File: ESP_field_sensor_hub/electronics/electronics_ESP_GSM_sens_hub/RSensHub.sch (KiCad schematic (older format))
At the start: 39 parts, among them J1 RJ45_Shielded, J2 RJ45_Shielded, J3 Conn_01x02_Female, J4 Conn_01x04_Female, Q1 IRF3205, Q2 IRF3205, Q3 IRF3205, Q4 IRF3205, Q5 IRF3205, Q6 IRF3205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

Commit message: Previous
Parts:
- added D? (x2): LED, symbol Device:LED
- added R? (x2): R, myComponents:resistor0.25,9mm, symbol Device:R
- added SW?: SW_DIP_x03, symbol Switch:SW_DIP_x03
- U4: footprint (none) -> myComponents:sim7000G_dev_board
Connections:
- net labels added: COM_IN_LED, COM_OUT_LED, SIM_IN_LED, SIM_OUT_LED
- wire segments 149 -> 182
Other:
- moved on the sheet: C1, D1, D2, D3, D4, D5, R1, R13, R14, R2, R4, R8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

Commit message: worked on sens hub PCB
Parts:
- removed D? (x2): LED, symbol Device:LED
- removed R?: R, myComponents:resistor0.25,9mm, symbol Device:R
- removed SW1, SW?: SW_DIP_x03, symbol Switch:SW_DIP_x03
- added AE1: Antenna, myComponents:GNSSantennaVertical, symbol Device:Antenna
- added C2: 1000u16V, myComponents:CAP_Radial_D10.0mm_P5.00mm, symbol Device:CP1
- added D6, D7: LED, myComponents:LED_small_D3.0mm, symbol Device:LED
- added J5: Barrel_Jack_MountingPin, symbol Connector:Barrel_Jack_MountingPin
- added J6: Conn_01x04_Female, myComponents:TerminalBlockRemovablex4, symbol Connector:Conn_01x04_Female
- added JP3, JP4, JP5, JP6: Jumper_2_Bridged, myComponents:jumperx2_P2.54mm_widePads, symbol Jumper:Jumper_2_Bridged
- added R17: R, myComponents:resistor0.25,9mm, symbol Device:R
- D1, D2, D4, D5: footprint (none) -> myComponents:LED_small_D3.0mm
- JP2: footprint (none) -> Jumper:SolderJumper-2_P1.3mm_Open_RoundedPad1.0x1.5mm
- gave numbers to parts that had none: 1
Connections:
- wire segments 182 -> 178
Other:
- moved on the sheet: D1, J4, JP1, R1, R18, R2, U1

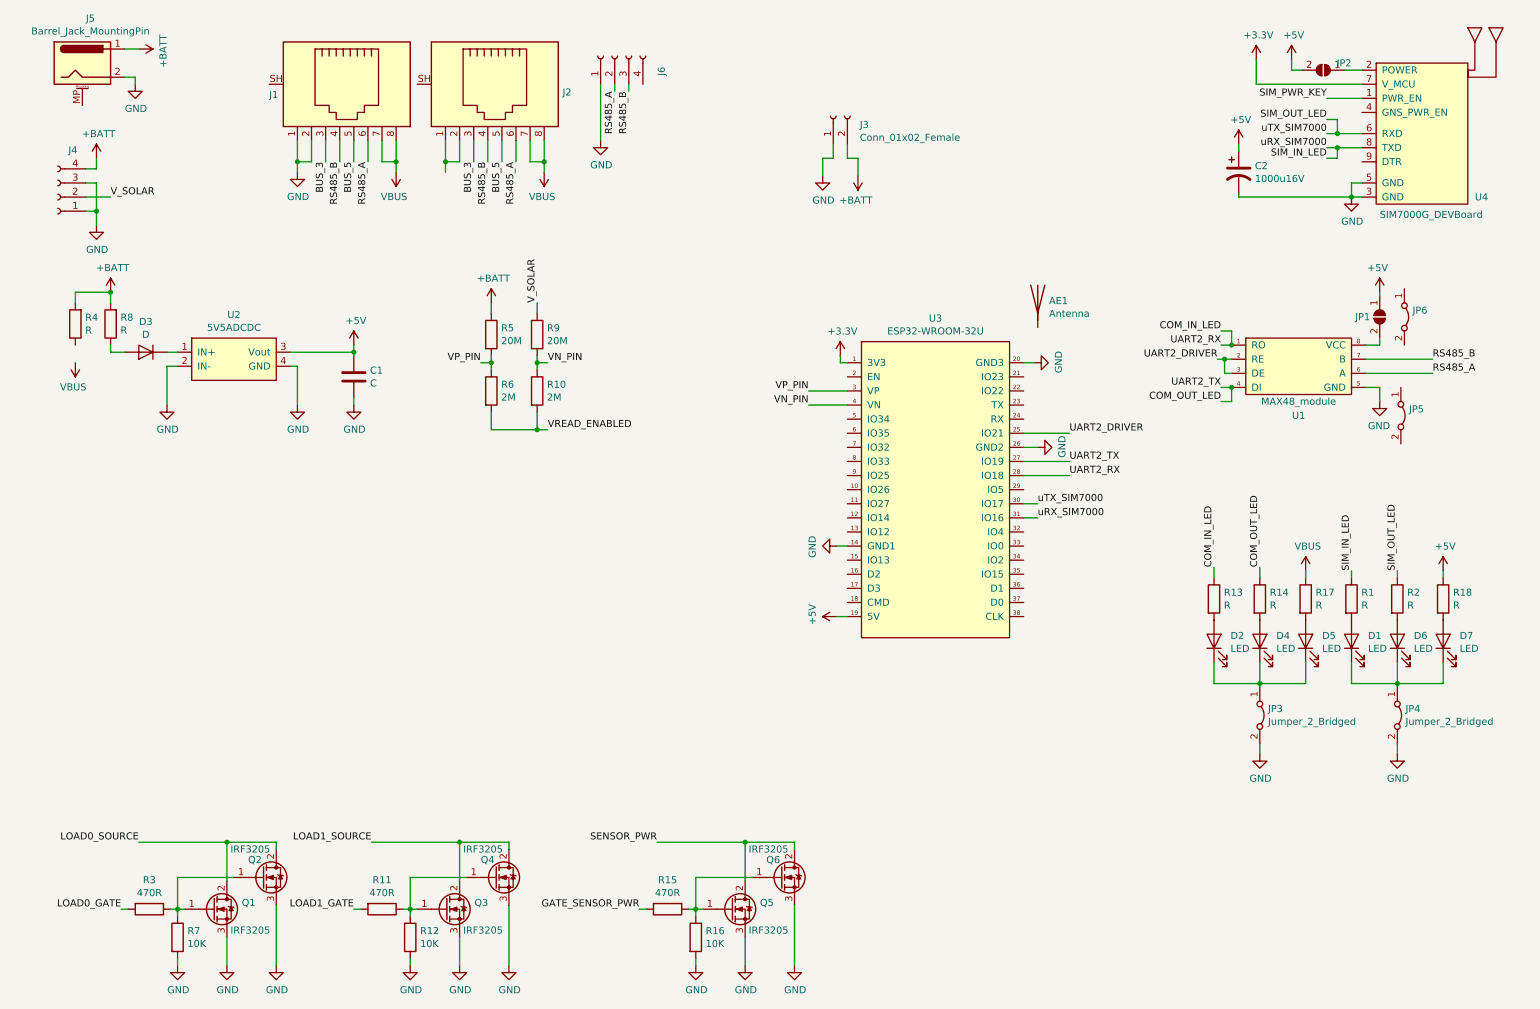
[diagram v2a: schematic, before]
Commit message: short circuit protection - tested on dot board, ESP control pins not connected
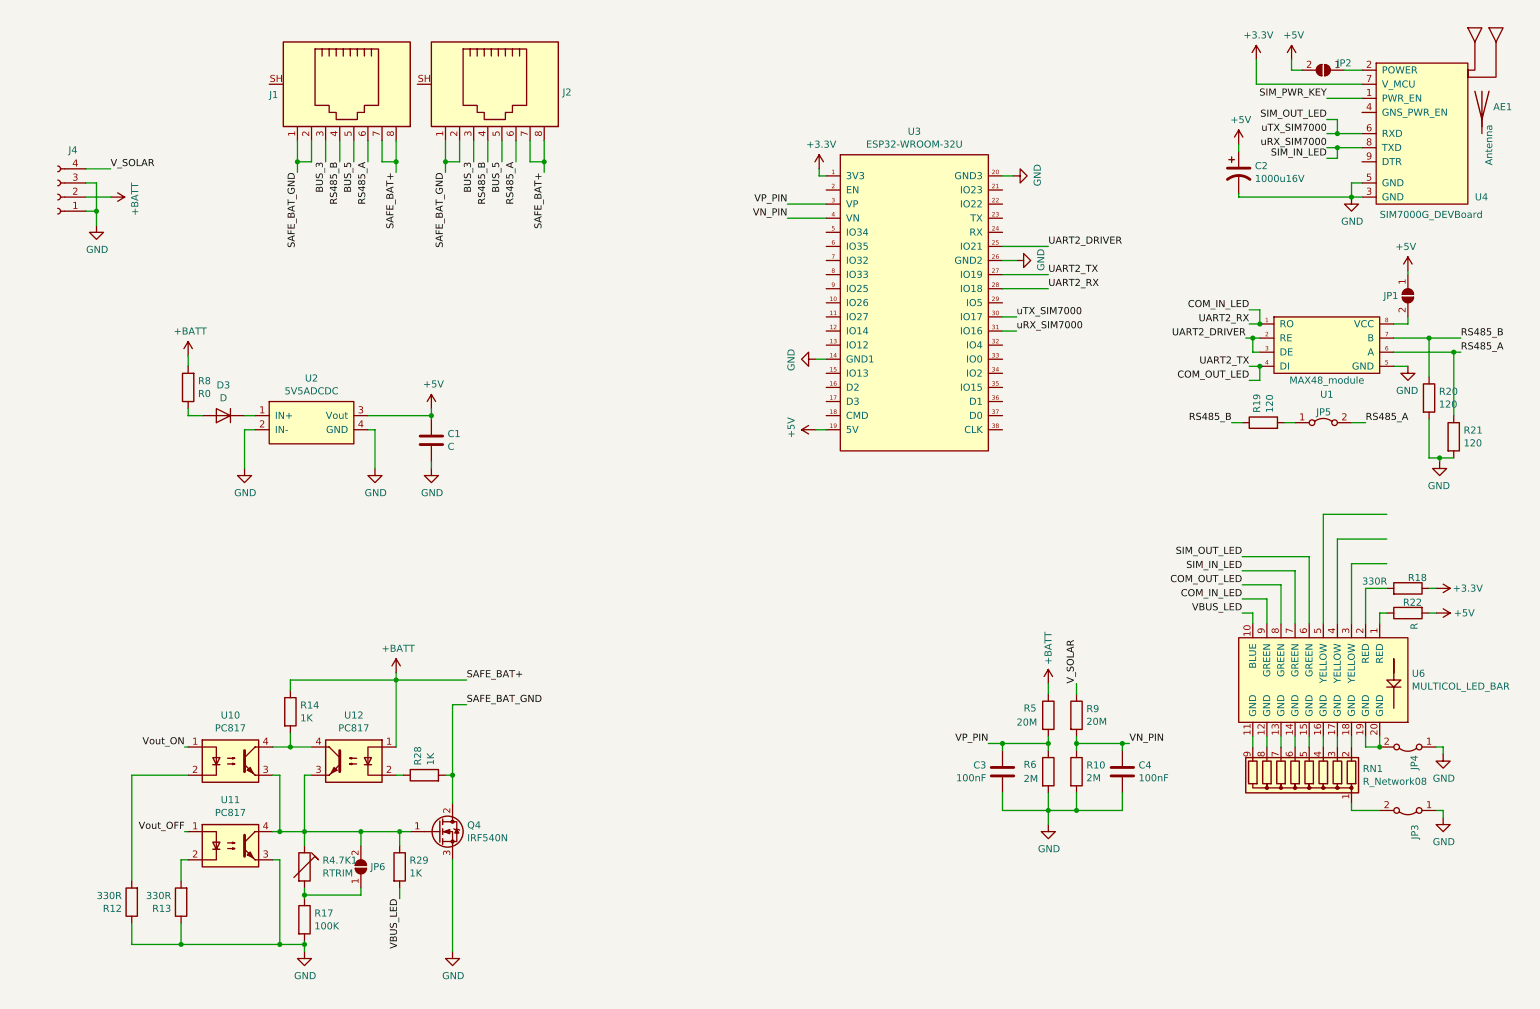
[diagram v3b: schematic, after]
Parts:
- removed D1, D2, D4, D5, D6, D7: LED, myComponents:LED_small_D3.0mm, symbol Device:LED
- removed J3: Conn_01x02_Female, symbol Connector:Conn_01x02_Female
- removed J5: Barrel_Jack_MountingPin, symbol Connector:Barrel_Jack_MountingPin
- removed J6: Conn_01x04_Female, myComponents:TerminalBlockRemovablex4, symbol Connector:Conn_01x04_Female
- removed JP6: Jumper_2_Bridged, myComponents:jumperx2_P2.54mm_widePads, symbol Jumper:Jumper_2_Bridged
- removed Q1, Q2, Q3, Q4, Q5, Q6: IRF3205, Package_TO_SOT_THT:TO-220-3_Vertical, symbol Transistor_FET:IRF3205
- removed R1, R2: R, myComponents:resistor0.25,9mm, symbol Device:R
- removed R11, R15, R3: 470R, myComponents:resistor0.25,9mm, symbol Device:R
- removed R16, R7: 10K, myComponents:resistor0.25,9mm, symbol Device:R
- removed R4: R, symbol Device:R
- added C3, C4: 100nF, myComponents:Capker_L4.6mm_W2.0mm_P2.50mm, symbol Device:C
- added JP6: SolderJumper_2_Open, Jumper:SolderJumper-2_P1.3mm_Open_RoundedPad1.0x1.5mm, symbol Jumper:SolderJumper_2_Open
- added Q4: IRF540N, myComponents:TO-220-3_Horizontal_TabDown_bothSides, symbol Transistor_FET:IRF540N
- added R19, R20, R21: 120, myComponents:resistor0.25,9mm, symbol Device:R
- added R22: R, myComponents:resistor0.25,9mm, symbol Device:R
- added R28, R29: 1K, myComponents:resistor0.25,9mm, symbol Device:R
- added R4.7K1: RTRIM, symbol Device:RTRIM
- added RN1: R_Network08, myComponents:PinHeader_1x9_P2.54mm_widePads, symbol Device:R_Network08
- added U10, U11, U12: PC817, myComponents:optoCouplerDIP4, symbol Isolator:PC817
- added U6: MULTICOL_LED_BAR, myComponents:DIP-20_LED_BAR_DISP, symbol myComponents:MULTICOL_LED_BAR
- JP1: footprint (none) -> Jumper:SolderJumper-2_P1.3mm_Open_RoundedPad1.0x1.5mm
- JP5: value Jumper_2_Bridged -> RS485 terminator
- R12: value 10K -> 330R
- R13, R18: value R -> 330R
- R14: value R -> 1K
- R17: value R -> 100K
- R8: value R -> R0; footprint (none) -> myComponents:resistor0.25,9mm
- U2: footprint (none) -> myComponents:DCDC_HCW_P715
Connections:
- net VREAD_ENABLED is gone; now on net GND: R10.2, R6.2
- net +3V3: now also R18.1
- net +5V: now also R22.2; no longer R18.1
- net +BATT: now also J1.7, J1.8, J2.7, J2.8, J4.2 (Pin_2), R14.1, U12.1; no longer J4.4 (Pin_4)
- net COM_IN_LED: now also U6.9 (GREEN); no longer R13.1
- net COM_OUT_LED: now also U6.8 (GREEN); no longer R14.1
- net GND: now also JP3.1 (A), JP4.1 (A), R12.1, R13.1, R17.2, C3.2, C4.2, Q4.3 (S), R20.2, R21.2, U11.3; no longer J1.1, J1.2, JP3.2 (B), JP4.2 (B), R12.2
- net RS485_A: now also JP5.2 (B), R21.1
- net RS485_B: now also R19.1, R20.1
- net SIM_IN_LED: now also U6.7 (GREEN)
- net SIM_OUT_LED: now also U6.6 (GREEN)
- net VN_PIN: now also C4.1
- net VP_PIN: now also C3.1
- net V_SOLAR: now also J4.4 (Pin_4); no longer J4.2 (Pin_2)
- net SAFE_BAT_GND: now reaches J2.1, J2.2
- net SAFE_BAT_GND: now also J1.1, J1.2, Q4.2 (D), R28.2
- net at R18.2: now also U6.2 (RED)
- net at R13.2: now also U11.2
- net at R14.2: now also U10.4, U12.4
- net at JP5.1 (A): now also R19.2
- removed net VBUS: J1.7, J1.8, J2.7, J2.8, R17.1
- new net: R22.1, U6.1 (RED)
- new net: RN1.9 (R8), U6.11 (GND)
- new net: RN1.8 (R7), U6.12 (GND)
- new net: RN1.7 (R6), U6.13 (GND)
- new net: RN1.6 (R5), U6.14 (GND)
- new net: RN1.5 (R4), U6.15 (GND)
- new net: RN1.4 (R3), U6.16 (GND)
- new net: RN1.3 (R2), U6.17 (GND)
- new net: RN1.2 (R1), U6.18 (GND)
- new net: JP4.2 (B), U6.19 (GND), U6.20 (GND)
- new net: JP6.2 (B), Q4.1 (G), R29.1, R4.7K1.1, U10.3, U11.4, U12.3
- new net: JP3.2 (B), RN1.1 (common)
- new net: R12.2, U10.2
- new net: R28.1, U12.2
- new net: JP6.1 (A), R17.1, R4.7K1.2
- new net VBUS_LED: R29.2, U6.10 (BLUE)
- new net Vout_OFF: U11.1
- new net Vout_ON: U10.1
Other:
- moved on the sheet: AE1, C1, D3, JP1, R10, R5, R6, R8, R9, U1, U2, U3
